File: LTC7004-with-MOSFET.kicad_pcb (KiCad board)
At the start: 2 copper layers, 25.3 x 32.7 mm, 10 parts, among them J1 Conn_01x02, J2 Grove-I2C-connector, Q1 Q_NMOS_SGD, U1 GateDriver_LTC7004

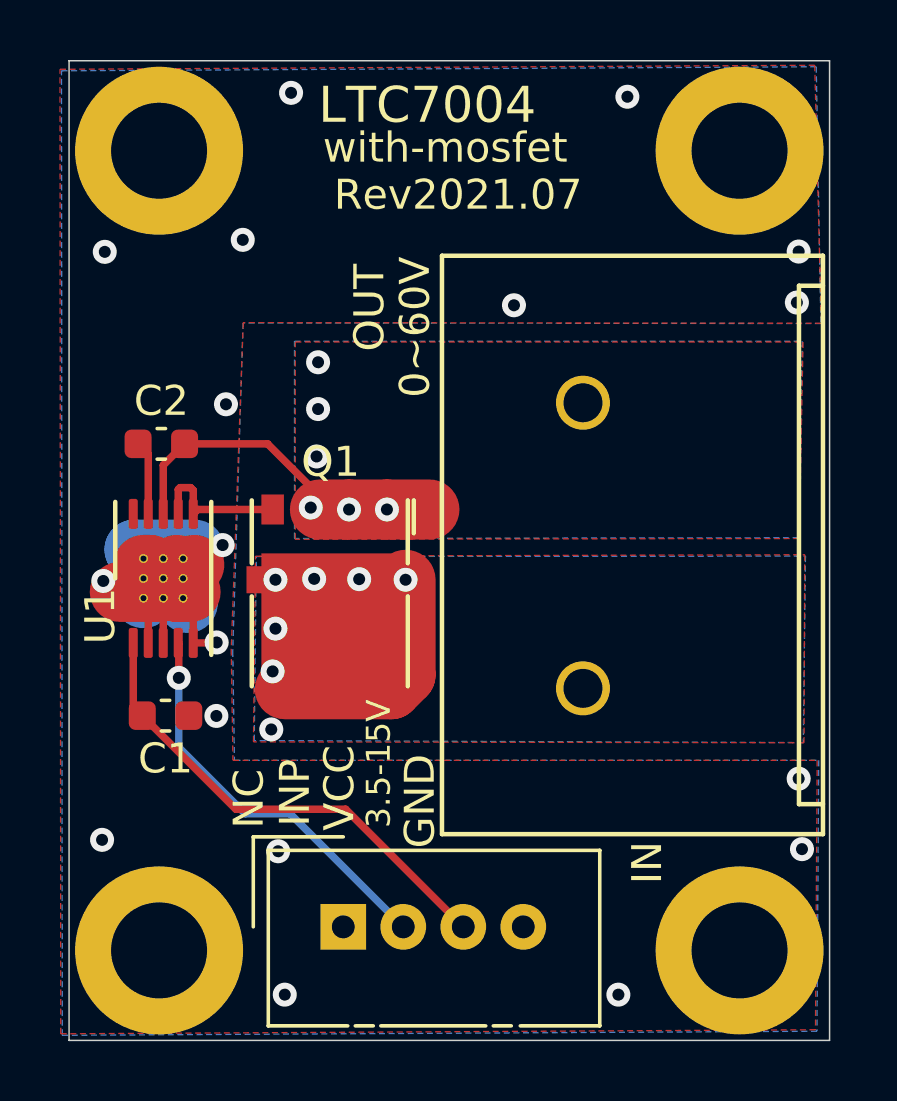
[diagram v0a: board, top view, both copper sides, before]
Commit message: Add second mosfet
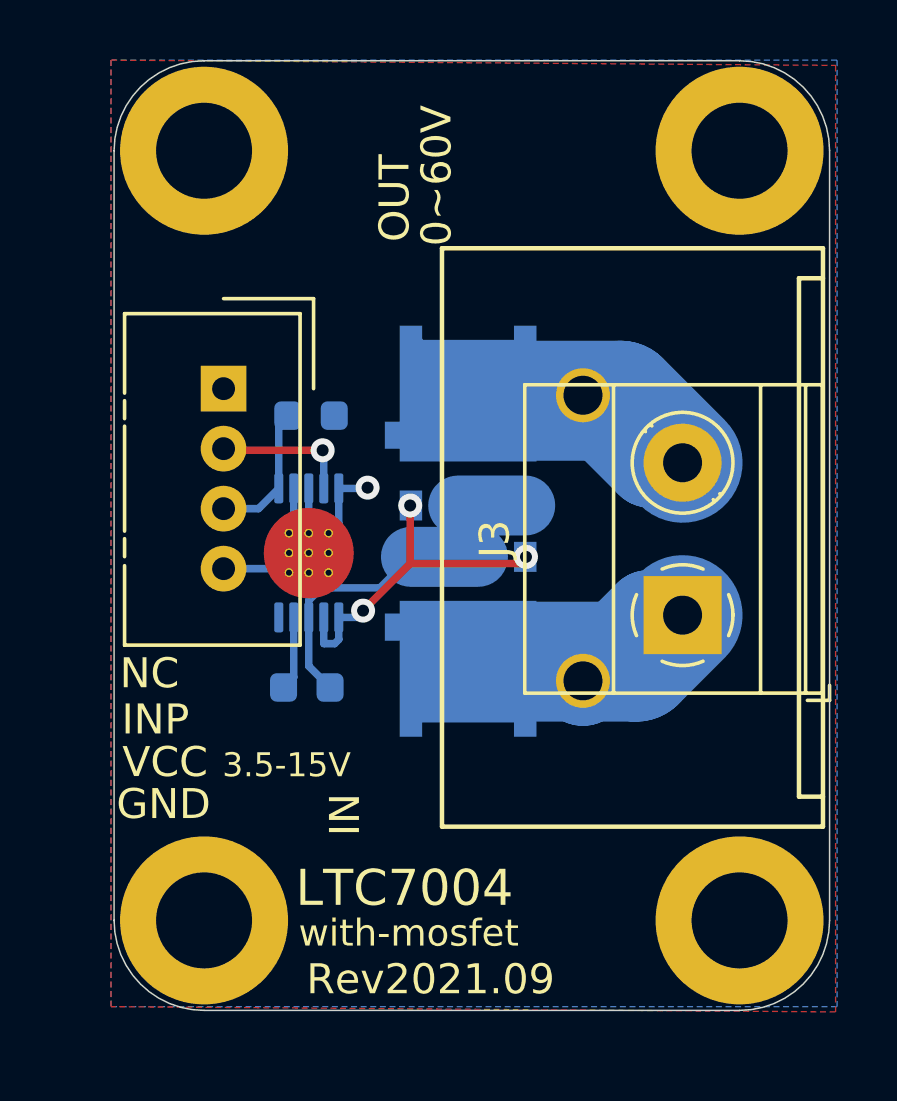
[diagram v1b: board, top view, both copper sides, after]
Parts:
- removed the REF** at (167.3, 79.8)
- removed the REF** at (167.3, 106.5)
- added J3: Conn_01x02, TerminalBlock_Phoenix:TerminalBlock_Phoenix_MKDS-1,5-2-5.08_1x02_P5.08mm_Horizontal, F.Cu at (184.8, 95.3)
- added Q2: Q_NMOS_SGD, my-kicad-footprints:DFN5, B.Cu at (177.6, 96.2)
- added REF**: MountingHole_3.2mm_M3_DIN965_Pad, MountingHole:MountingHole_3.2mm_M3_DIN965_Pad, F.Cu at (168.8, 79.8)
- added REF**: MountingHole_3.2mm_M3_DIN965_Pad, MountingHole:MountingHole_3.2mm_M3_DIN965_Pad, F.Cu at (168.8, 105.5)
- C1, C2, Q1, U1: moved to B.Cu
- moved J2 18.4 mm to (169.4, 87.8), turned to 0 degrees
- moved C1 11.1 mm to (172.4, 88.7)
- moved C2 9.46 mm to (172.2, 97.7)
- moved Q1 7.35 mm to (177.6, 88.8)
- moved U1 4.92 mm to (172.3, 93.2)
- moved REF** 1.00 mm to (186.7, 105.5)
- moved J1 0.25 mm to (181.4, 97.5)
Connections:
- C2 pad 2: /PowerOut -> /PowerSense
- J1 pad 1: /PowerIn -> /PowerOut
- J1 pad 2: /PowerOut -> /PowerIn
- Q1 pad 1: /PowerOut -> /PowerSense
- U1 pad 8: /PowerOut -> /PowerSense
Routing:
- net /PowerOut: track 11.8 -> 25.4 mm, vias 6 -> 0
- net /PowerSense: track 0.00 -> 13.4 mm
- net VCC: track 16.2 -> 4.67 mm
- net /INP: track 13.5 -> 4.61 mm
- net /PowerIn: track 19.5 -> 28.3 mm, vias 7 -> 0
- net GND: track 19.1 -> 12.7 mm, vias 18 -> 1
- net /Gate: track 4.87 -> 11.2 mm, vias 0 -> 3
- removed copper zone on B.Cu, net /PowerIn
- removed copper zone on F.Cu, net /PowerIn
- removed copper zone on B.Cu, net /PowerOut
- removed copper zone on F.Cu, net /PowerOut
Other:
- board size 25.3 x 32.7 mm -> 23.8 x 31.7 mm
- board text added: "Rev2021.09"
- board text removed: "Rev2021.07"

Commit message: Add condensor, resistor and varistor
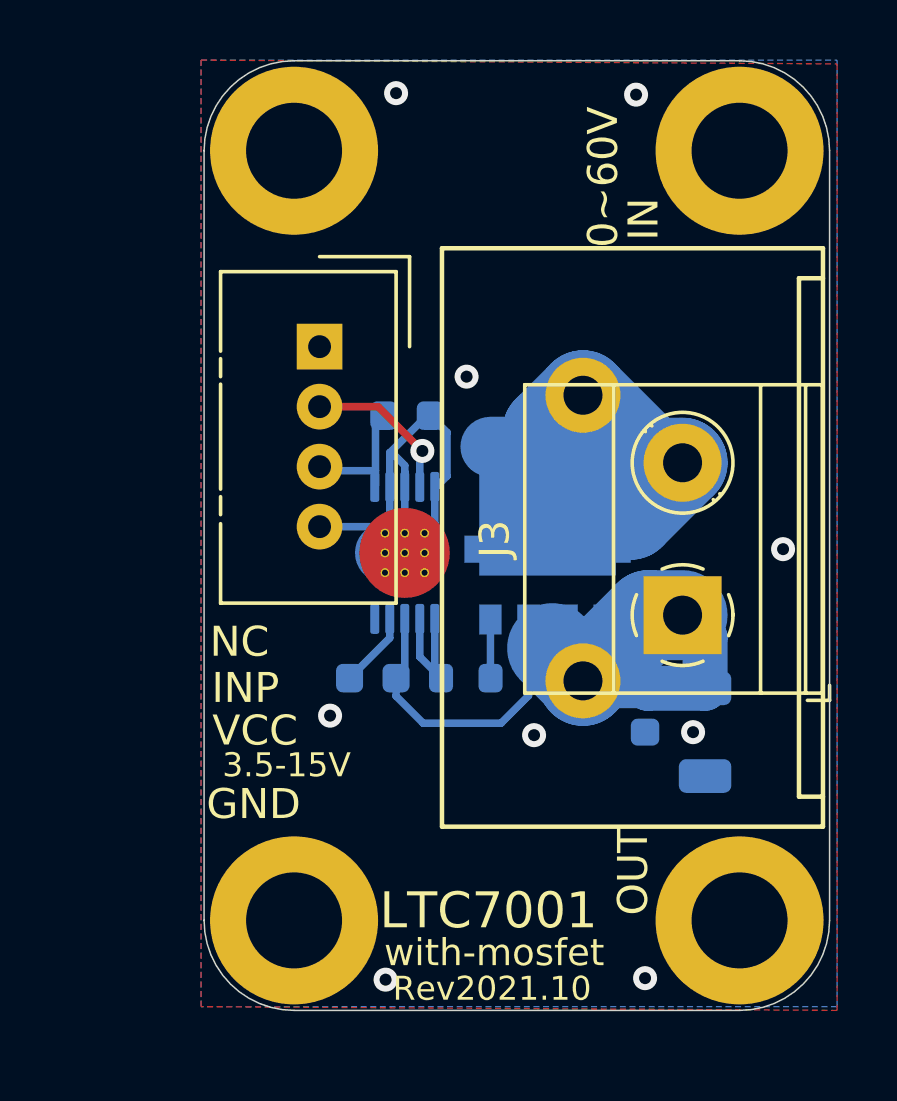
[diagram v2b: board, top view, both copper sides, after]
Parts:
- removed Q2: Q_NMOS_SGD, my-kicad-footprints:DFN5
- removed the REF** at (168.8, 79.8)
- removed the REF** at (168.8, 105.5)
- added C3: 0.1uf, Capacitor_SMD:C_0603_1608Metric, B.Cu at (183.5, 98.4)
- added R1: 100, Resistor_SMD:R_0603_1608Metric, B.Cu at (177.5, 97.4)
- added REF**: MountingHole_3.2mm_M3_DIN965_Pad, MountingHole:MountingHole_3.2mm_M3_DIN965_Pad, F.Cu at (171.8, 79.8)
- added REF**: MountingHole_3.2mm_M3_DIN965_Pad, MountingHole:MountingHole_3.2mm_M3_DIN965_Pad, F.Cu at (171.8, 105.5)
- added RV1: Varistor, Resistor_SMD:R_1206_3216Metric, B.Cu at (185.5, 99.2)
- C1: value 0.1uf -> 1uf
- moved Q1 4.63 mm to (180.2, 92.7)
- moved J2 3.49 mm to (172.7, 86.3)
- moved U1 3.20 mm to (175.5, 93.2)
- moved C1 3.20 mm to (175.6, 88.7)
- moved C2 2.22 mm to (174.4, 97.4)
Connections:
- C2 pad 2: /PowerSense -> /PowerOut
- Q1 pad 1: /PowerSense -> /PowerOut
- Q1 pad 2: /Gate -> Net-(Q1-Pad2)
- U1 pad 8: /PowerSense -> /PowerOut
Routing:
- net /PowerSense: track 13.4 -> 0.00 mm
- net /PowerIn: track 28.3 -> 19.1 mm
- net /Gate: track 11.2 -> 4.43 mm, vias 3 -> 0
- net GND: track 12.7 -> 18.9 mm, vias 1 -> 9
- net /PowerOut: track 25.4 -> 23.1 mm
- net Net-(Q1-Pad2): track 0.00 -> 1.96 mm
- net /INP: track 4.61 -> 5.27 mm
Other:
- board size 23.8 x 31.7 mm -> 20.8 x 31.7 mm
- board text added: "LTC7001"
- board text added: "Rev2021.10"
- board text removed: "LTC7004"
- board text removed: "Rev2021.09"
